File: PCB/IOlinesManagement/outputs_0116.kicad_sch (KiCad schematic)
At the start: 208 parts, among them Q17 BC817, Q18 BC817, Q19 BC337, Q20 BC327, Q21 BC327, Q22 BC337, Q23 BC817, Q24 BC817, Q26 BC817, Q27 BC337, Q28 BC327, Q29 BC817, Q30 BC817, Q31 BC817, Q32 BC337, Q33 BC327, Q35 BC817, Q36 BC817, Q37 BC337, Q38 BC327, Q39 BC817, Q40 BC817, Q41 BC337, Q42 BC327, Q43 BC817, Q44 BC817, Q45 BC337, Q46 BC327, Q47 BC817, Q48 BC817, Q49 BC337, Q50 BC327, Q65 BC817, Q66 BC817, Q67 BC817, Q68 BC817, Q69 BC337, Q70 BC337, Q71 BC327, Q72 BC327, Q73 BC817, Q74 BC817, Q75 BC817, Q76 BC817, Q77 BC337, Q78 BC337, Q79 BC327, Q80 BC327, Q81 BC817, Q82 BC817, Q83 BC817, Q84 BC817, Q85 BC337, Q86 BC337, Q87 BC327, Q88 BC327, Q89 BC817, Q90 BC817, Q91 BC817, Q92 BC817, Q93 BC337, Q94 BC337, Q95 BC327, Q96 BC327

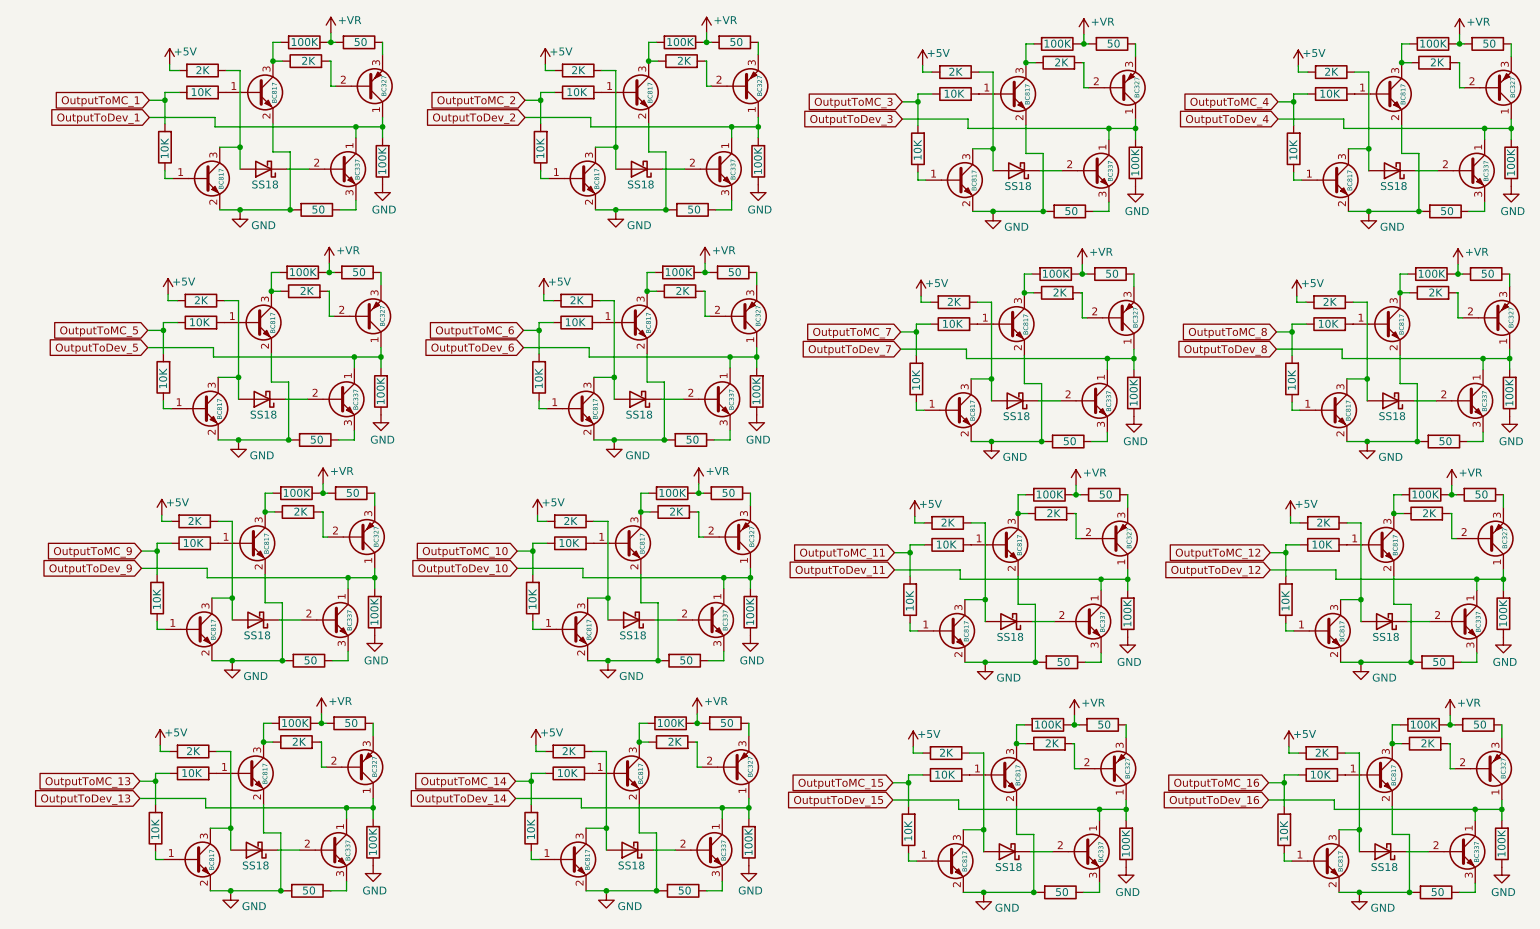
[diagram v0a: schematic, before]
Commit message: Enhancement: push-pull components-blocks have been replaced by MIC4427 devices
We are not more living in the 1990 age :-(
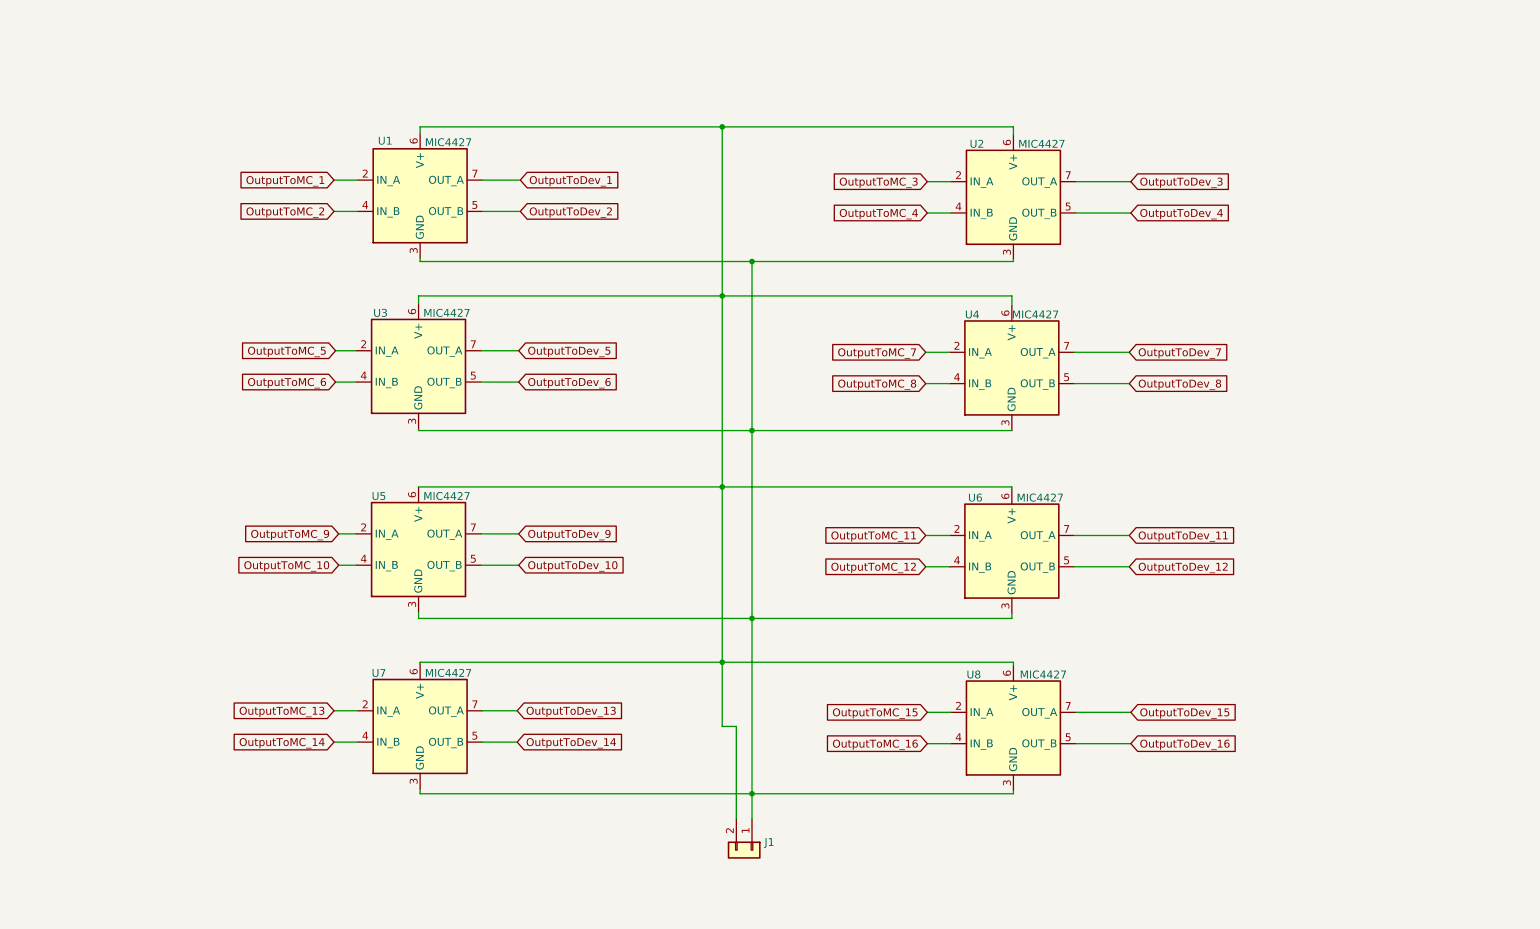
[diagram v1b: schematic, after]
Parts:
- removed D1, D10, D11, D12, D13, D14, D15, D16, D2, D3, D4, D5, D6, D7, D8, D9: SS18, Diode_SMD:D_SMA, symbol Diode:SS18
- removed Q17, Q18, Q23, Q24, Q26, Q29, Q30, Q31, Q35, Q36, Q39, Q40, Q43, Q44, Q47, Q48, Q65, Q66, Q67, Q68, Q73, Q74, Q75, Q76, Q81, Q82, Q83, Q84, Q89, Q90, Q91, Q92: BC817, Package_TO_SOT_SMD:SOT-23, symbol Transistor_BJT:BC817
- removed Q19, Q22, Q27, Q32, Q37, Q41, Q45, Q49, Q69, Q70, Q77, Q78, Q85, Q86, Q93, Q94: BC337, Package_TO_SOT_THT:TO-92_Inline_Wide, symbol Transistor_BJT:BC337
- removed Q20, Q21, Q28, Q33, Q38, Q42, Q46, Q50, Q71, Q72, Q79, Q80, Q87, Q88, Q95, Q96: BC327, Package_TO_SOT_THT:TO-92_Inline_Wide, symbol Transistor_BJT:BC327
- removed R100, R101, R102, R171, R172, R173, R174, R187, R188, R189, R190, R203, R204, R205, R206, R26, R27, R28, R32, R38, R39, R47, R48, R58, R59, R67, R68, R75, R76, R86, R87, R99: 50, Resistor_SMD:R_1206_3216Metric, symbol Device:R
- removed R103, R104, R167, R168, R17, R175, R176, R18, R183, R184, R191, R192, R199, R200, R207, R208, R24, R29, R36, R41, R45, R49, R53, R60, R64, R69, R73, R77, R81, R88, R95, R96: 100K, Resistor_SMD:R_1206_3216Metric, symbol Device:R
- removed R161, R162, R164, R166, R177, R178, R180, R182, R193, R194, R196, R198, R20, R21, R23, R30, R33, R35, R42, R44, R50, R52, R61, R63, R70, R72, R78, R80, R89, R90, R92, R94: 10K, Resistor_SMD:R_1206_3216Metric, symbol Device:R
- removed R163, R165, R169, R170, R179, R181, R185, R186, R19, R195, R197, R201, R202, R22, R25, R31, R34, R37, R43, R46, R51, R57, R62, R66, R71, R74, R79, R85, R91, R93, R97, R98: 2K, Resistor_SMD:R_1206_3216Metric, symbol Device:R
- added J1: Conn_01x02, Connector_PinHeader_2.54mm:PinHeader_1x02_P2.54mm_Vertical, symbol Connector_Generic:Conn_01x02
- added U1, U2, U3, U4, U5, U6, U7, U8: MIC4427, Package_SO:MSOP-8_3x3mm_P0.65mm, symbol Driver_FET:MIC4427
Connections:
- net OutputToDev_1: now also U1.7 (OUT_A)
- net OutputToDev_10: now also U5.5 (OUT_B)
- net OutputToDev_11: now also U6.7 (OUT_A)
- net OutputToDev_12: now also U6.5 (OUT_B)
- net OutputToDev_13: now also U7.7 (OUT_A)
- net OutputToDev_14: now also U7.5 (OUT_B)
- net OutputToDev_15: now also U8.7 (OUT_A)
- net OutputToDev_16: now also U8.5 (OUT_B)
- net OutputToDev_2: now also U1.5 (OUT_B)
- net OutputToDev_3: now also U2.7 (OUT_A)
- net OutputToDev_4: now also U2.5 (OUT_B)
- net OutputToDev_5: now also U3.7 (OUT_A)
- net OutputToDev_6: now also U3.5 (OUT_B)
- net OutputToDev_7: now also U4.7 (OUT_A)
- net OutputToDev_8: now also U4.5 (OUT_B)
- net OutputToDev_9: now also U5.7 (OUT_A)
- net OutputToMC_1: now also U1.2 (IN_A)
- net OutputToMC_10: now also U5.4 (IN_B)
- net OutputToMC_11: now also U6.2 (IN_A)
- net OutputToMC_12: now also U6.4 (IN_B)
- net OutputToMC_13: now also U7.2 (IN_A)
- net OutputToMC_14: now also U7.4 (IN_B)
- net OutputToMC_15: now also U8.2 (IN_A)
- net OutputToMC_16: now also U8.4 (IN_B)
- net OutputToMC_2: now also U1.4 (IN_B)
- net OutputToMC_3: now also U2.2 (IN_A)
- net OutputToMC_4: now also U2.4 (IN_B)
- net OutputToMC_5: now also U3.2 (IN_A)
- net OutputToMC_6: now also U3.4 (IN_B)
- net OutputToMC_7: now also U4.2 (IN_A)
- net OutputToMC_8: now also U4.4 (IN_B)
- net OutputToMC_9: now also U5.2 (IN_A)
- new net: J1.1 (Pin_1), U1.3 (GND), U2.3 (GND), U3.3 (GND), U4.3 (GND), U5.3 (GND), U6.3 (GND), U7.3 (GND), U8.3 (GND)
- new net: J1.2 (Pin_2), U1.6 (V+), U2.6 (V+), U3.6 (V+), U4.6 (V+), U5.6 (V+), U6.6 (V+), U7.6 (V+), U8.6 (V+)
